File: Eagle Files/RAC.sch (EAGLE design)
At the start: 9 parts

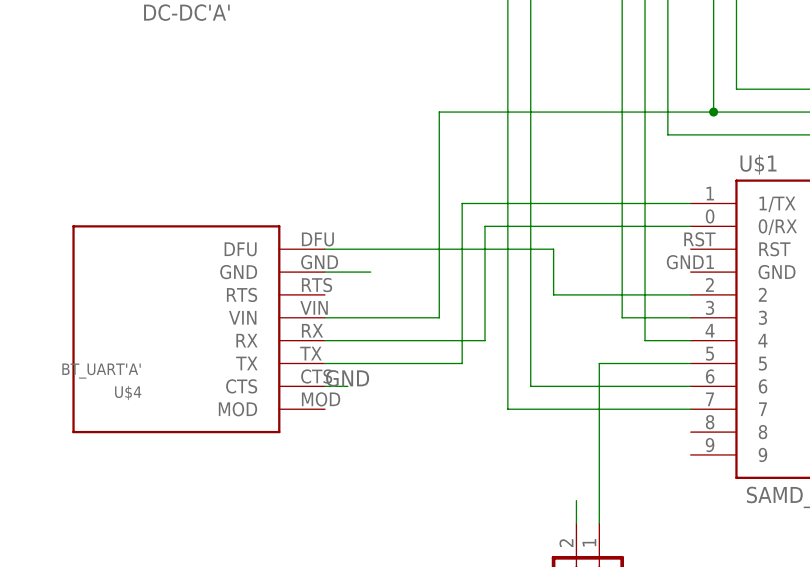
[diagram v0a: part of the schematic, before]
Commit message: Corrige inversión de pines TX y RX para BLE
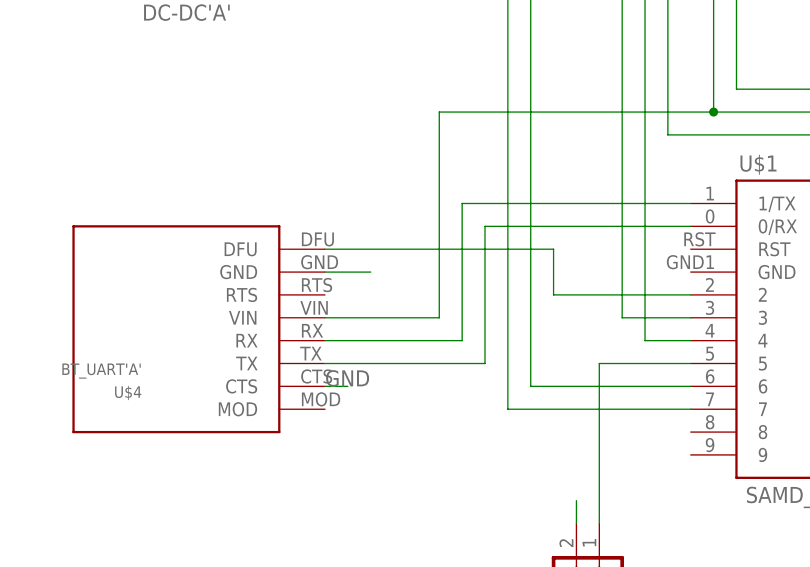
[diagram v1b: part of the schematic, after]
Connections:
- net N$17: now also U$4.TX; no longer U$4.RX
- net N$18: now also U$4.RX; no longer U$4.TX
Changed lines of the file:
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@@
 <net name="N$17" class="0">
 <segment>
-<pinref part="U$4" gate="G$1" pin="RX"/>
-<wire x1="-48.26" y1="48.26" x2="-30.48" y2="48.26" width="0.1524" layer="91"/>
-<wire x1="-30.48" y1="48.26" x2="-30.48" y2="60.96" width="0.1524" layer="91"/>
+<wire x1="-30.48" y1="45.72" x2="-30.48" y2="60.96" width="0.1524" layer="91"/>
 <pinref part="U$1" gate="G$1" pin="0/RX"/>
 <wire x1="-30.48" y1="60.96" x2="-7.62" y2="60.96" width="0.1524" layer="91"/>
+<pinref part="U$4" gate="G$1" pin="TX"/>
+<wire x1="-30.48" y1="45.72" x2="-48.26" y2="45.72" width="0.1524" layer="91"/>
 </segment>
 </net>
 <net name="N$18" class="0">
 <segment>
-<pinref part="U$4" gate="G$1" pin="TX"/>
-<wire x1="-48.26" y1="45.72" x2="-33.02" y2="45.72" width="0.1524" layer="91"/>
-<wire x1="-33.02" y1="45.72" x2="-33.02" y2="63.5" width="0.1524" layer="91"/>
 <pinref part="U$1" gate="G$1" pin="1/TX"/>
 <wire x1="-33.02" y1="63.5" x2="-7.62" y2="63.5" width="0.1524" layer="91"/>
+<wire x1="-33.02" y1="63.5" x2="-33.02" y2="48.26" width="0.1524" layer="91"/>
+<pinref part="U$4" gate="G$1" pin="RX"/>
+<wire x1="-33.02" y1="48.26" x2="-48.26" y2="48.26" width="0.1524" layer="91"/>
 </segment>
 </net>
